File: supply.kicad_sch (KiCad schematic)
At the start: 93 parts, among them IC12 74HC00PW, IC13 SN74LVC1G126DCKR, IC4 TPS7A0518PDBVT, J12 533980471, T3 BSS138APW, U1 LM3671MF-3.3/NOPB, U2 LM62440-Q1, U3 SN74LXC1T45DBVR, U5 LM3671MF-3.3/NOPB, U6 SIC477ED-T1-GE3

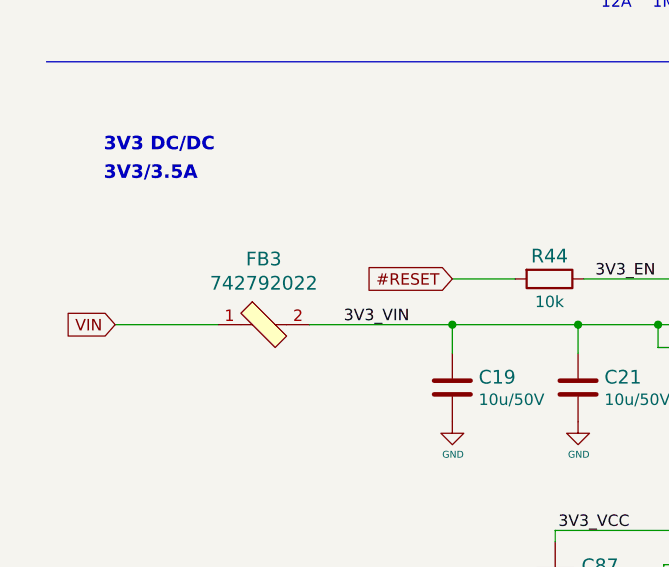
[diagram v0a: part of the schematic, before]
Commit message: Replaced 742792022 ferrites with 74279220181 for higher current capability
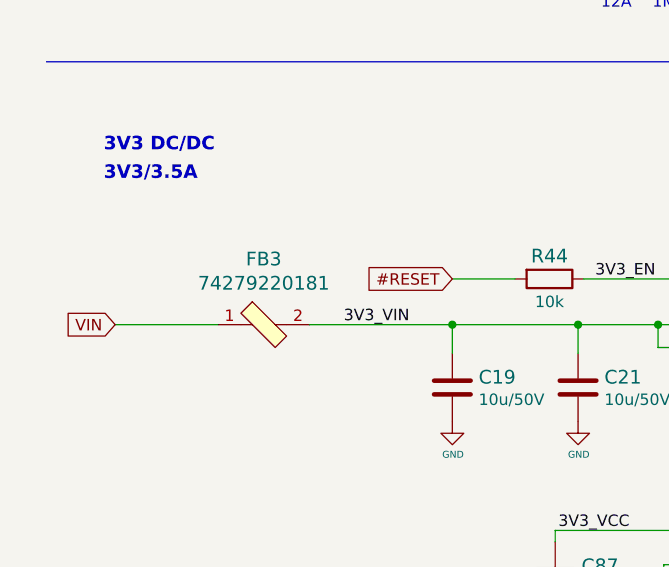
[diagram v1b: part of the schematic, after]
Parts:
- FB3: value 742792022 -> 74279220181; symbol jetson-nano-baseboard:742792022 -> jetson-nano-baseboard:74279220181; MPN 742792022 -> 74279220181
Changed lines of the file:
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@@
     (pin "1")
   )
-  (symbol (lib_id "jetson-nano-baseboard:742792022") (at 40.64 136.525 0) (unit 1)
+  (symbol (lib_id "jetson-nano-baseboard:74279220181") (at 40.64 136.525 0) (unit 1)
     (in_bom yes) (on_board yes)
     (property "Reference" "FB3" (id 0) (at 40.64 129.2352 0)
       (effects (font (size 1.524 1.524)))
     )
-    (property "Value" "742792022" (id 1) (at 40.64 131.9276 0)
+    (property "Value" "74279220181" (id 1) (at 40.64 131.9276 0)
       (effects (font (size 1.524 1.524)))
     )
@@
       (effects (font (size 1.524 1.524)) (justify left) hide)
     )
-    (property "Datasheet" "https://www.we-online.com/katalog/datasheet/742792022.pdf" (id 3) (at 45.72 128.905 0)
+    (property "Datasheet" "https://www.we-online.com/components/products/datasheet/74279220181.pdf" (id 3) (at 45.72 128.905 0)
       (effects (font (size 1.524 1.524)) (justify left) hide)
     )
-    (property "MPN" "742792022" (id 4) (at 45.72 123.825 0)
+    (property "MPN" "74279220181" (id 4) (at 45.72 123.825 0)
       (effects (font (size 1.524 1.524)) (justify left) hide)
     )

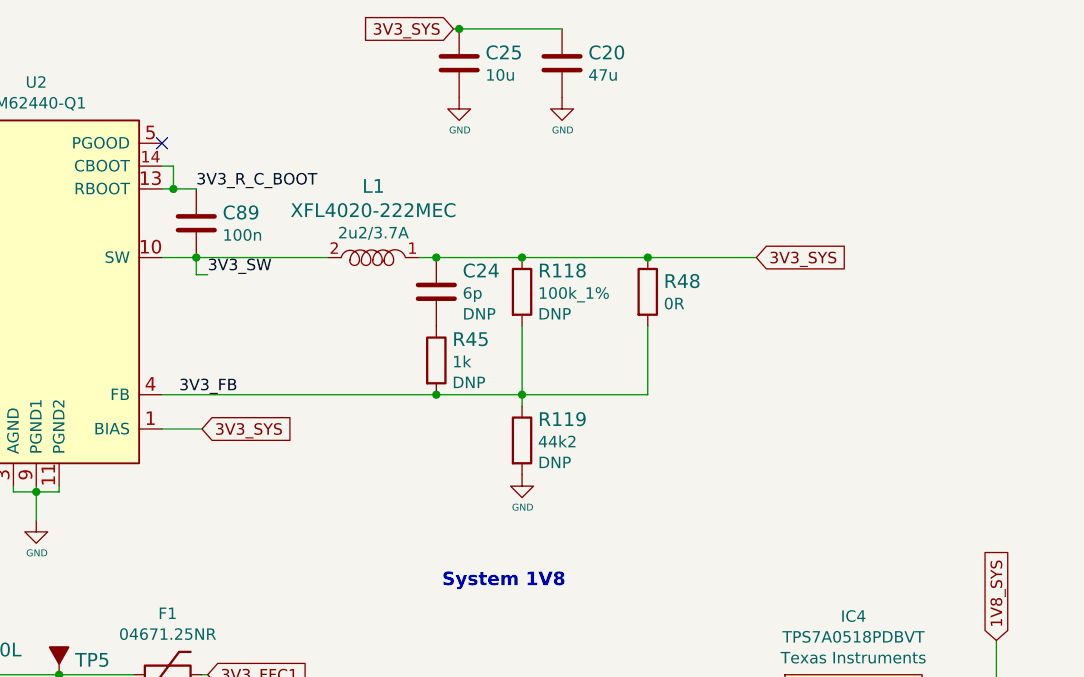
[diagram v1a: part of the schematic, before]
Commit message: Added resistor between RBOOT and CBOOT on 3V3_SYS regulator for reduced EMI
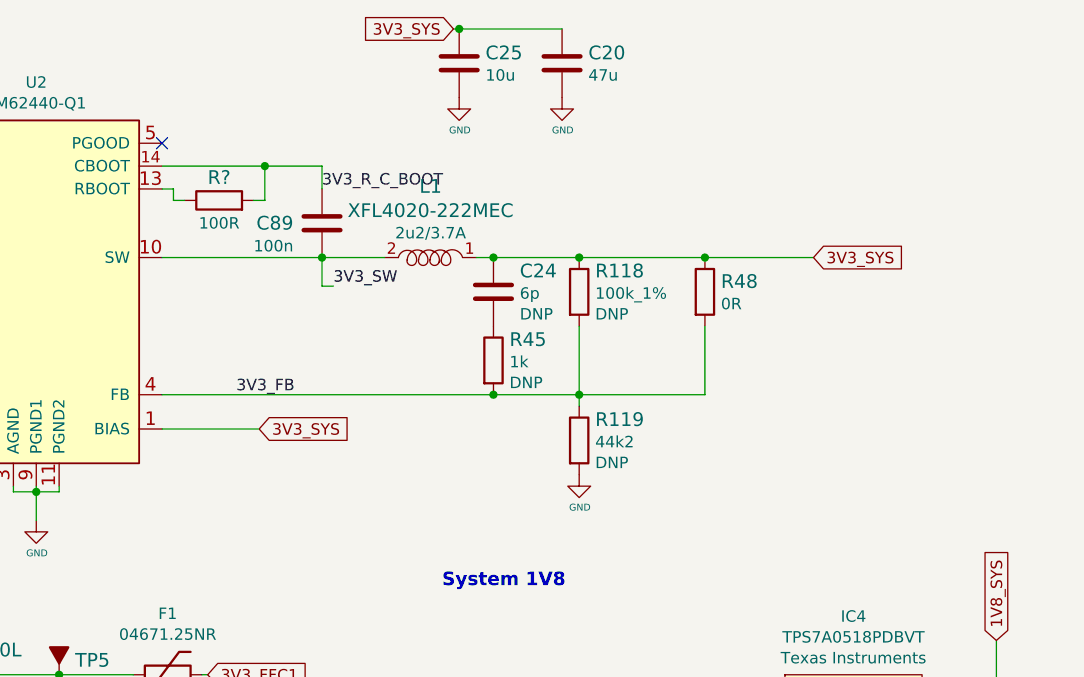
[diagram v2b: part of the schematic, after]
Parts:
- added R?: R_100R_0402, antmicro-footprints:0402-res, symbol antmicroResistors0402:R_100R_0402
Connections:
- net 3V3_R_C_BOOT: now also R?.2; no longer U2.13 (RBOOT)
- new net: R?.1, U2.13 (RBOOT)
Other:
- moved on the sheet: C24, C89, L1, R118, R119, R45, R48

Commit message: Added CAN interface
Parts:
- R?: footprint antmicro-footprints:0402-res -> jetson-nano-baseboard-footprints:0402-res; symbol antmicroResistors0402:R_100R_0402 -> jetson-nano-baseboard:R_100R_0402
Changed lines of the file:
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@@
     (pin "2")
   )
-  (symbol (lib_id "antmicroResistors0402:R_100R_0402") (at 120.015 137.795 0) (unit 1)
+  (symbol (lib_id "jetson-nano-baseboard:R_100R_0402") (at 120.015 137.795 0) (unit 1)
     (in_bom yes) (on_board yes)
     (property "Reference" "R?" (id 0) (at 120.015 135.255 0)
@@
       (effects (font (size 1.524 1.524)) hide)
     )
-    (property "Footprint" "antmicro-footprints:0402-res" (id 2) (at 125.095 132.715 0)
+    (property "Footprint" "jetson-nano-baseboard-footprints:0402-res" (id 2) (at 125.095 132.715 0)
       (effects (font (size 1.524 1.524)) (justify left) hide)
     )

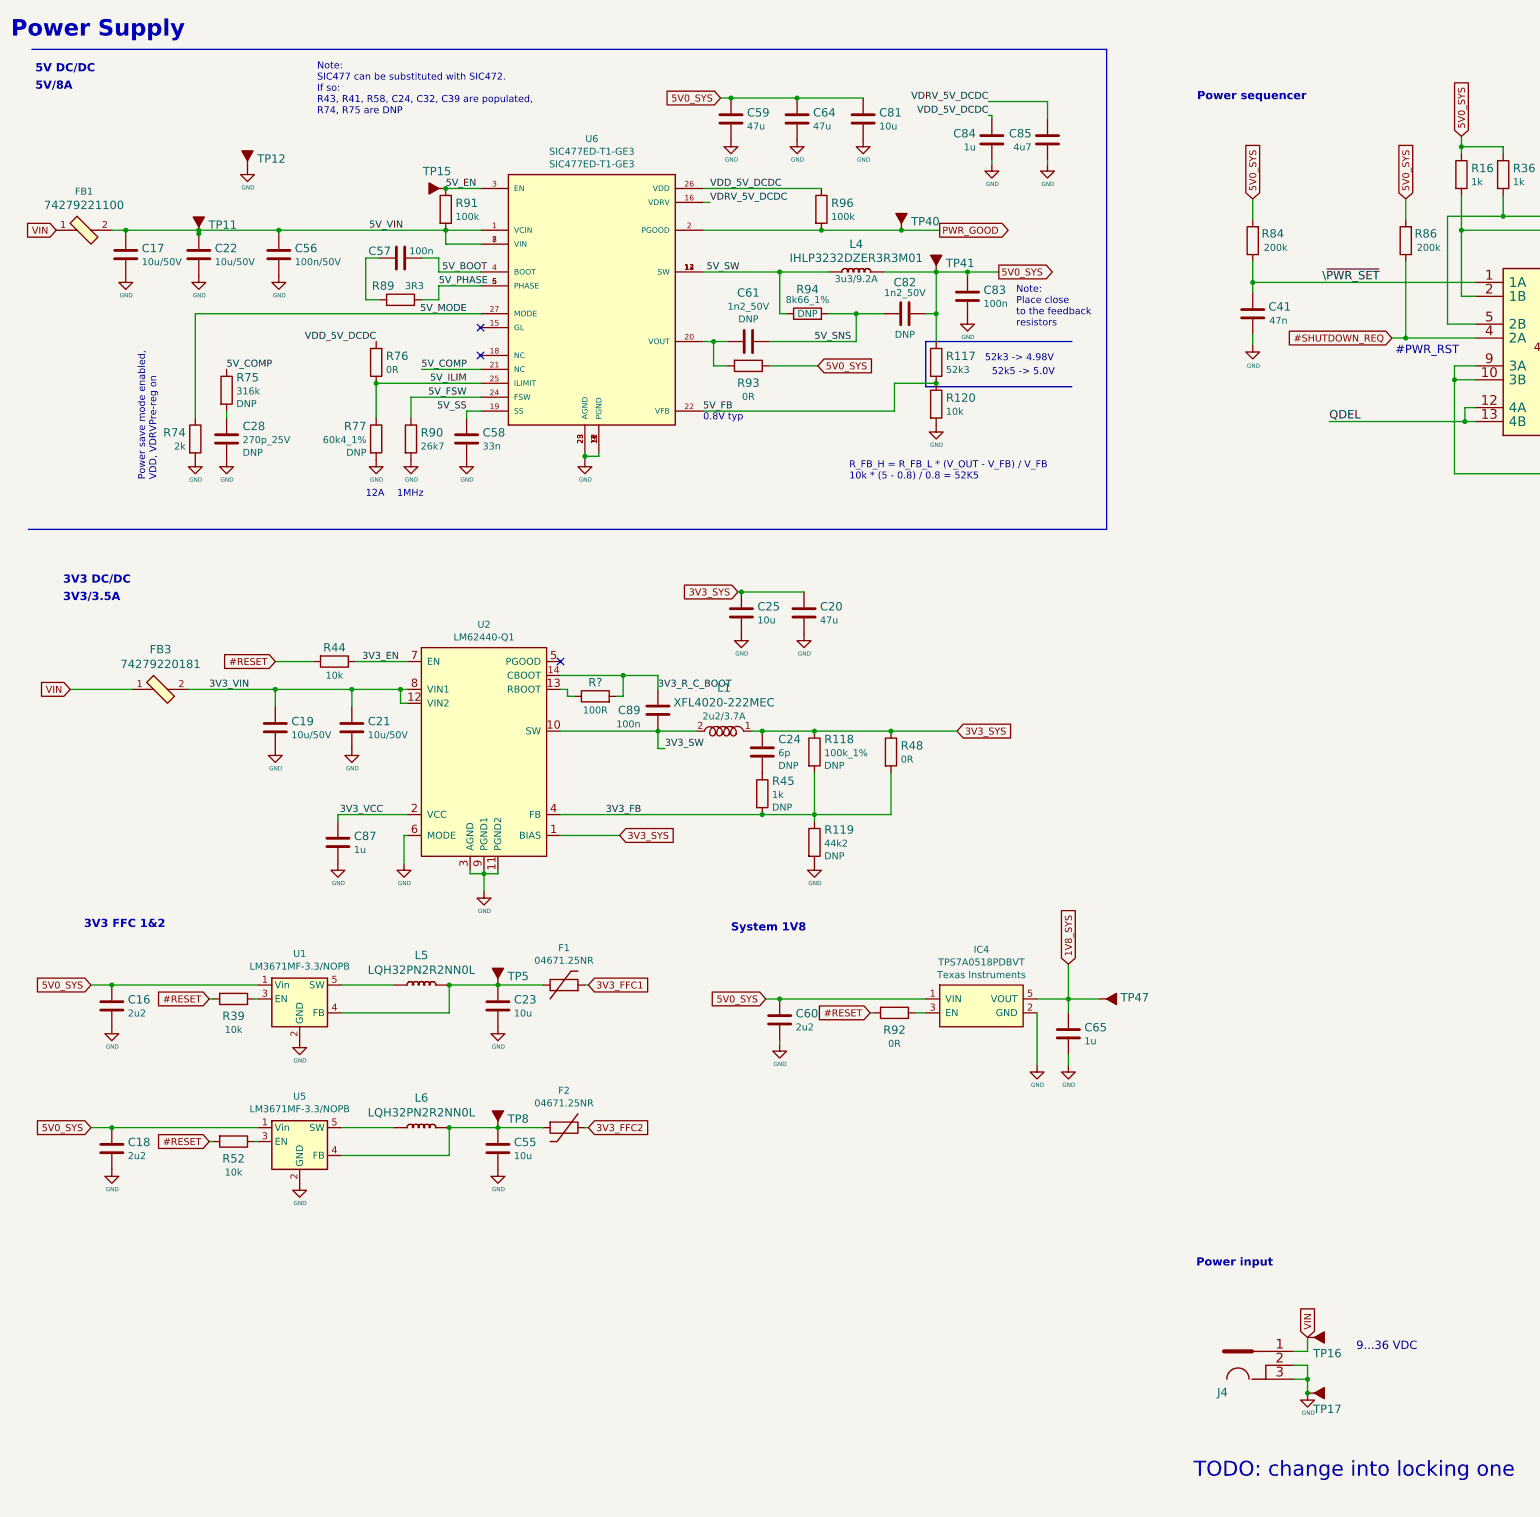
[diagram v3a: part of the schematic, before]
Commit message: Improved input protection - added TVSes, reverse polarity protection and input fuse
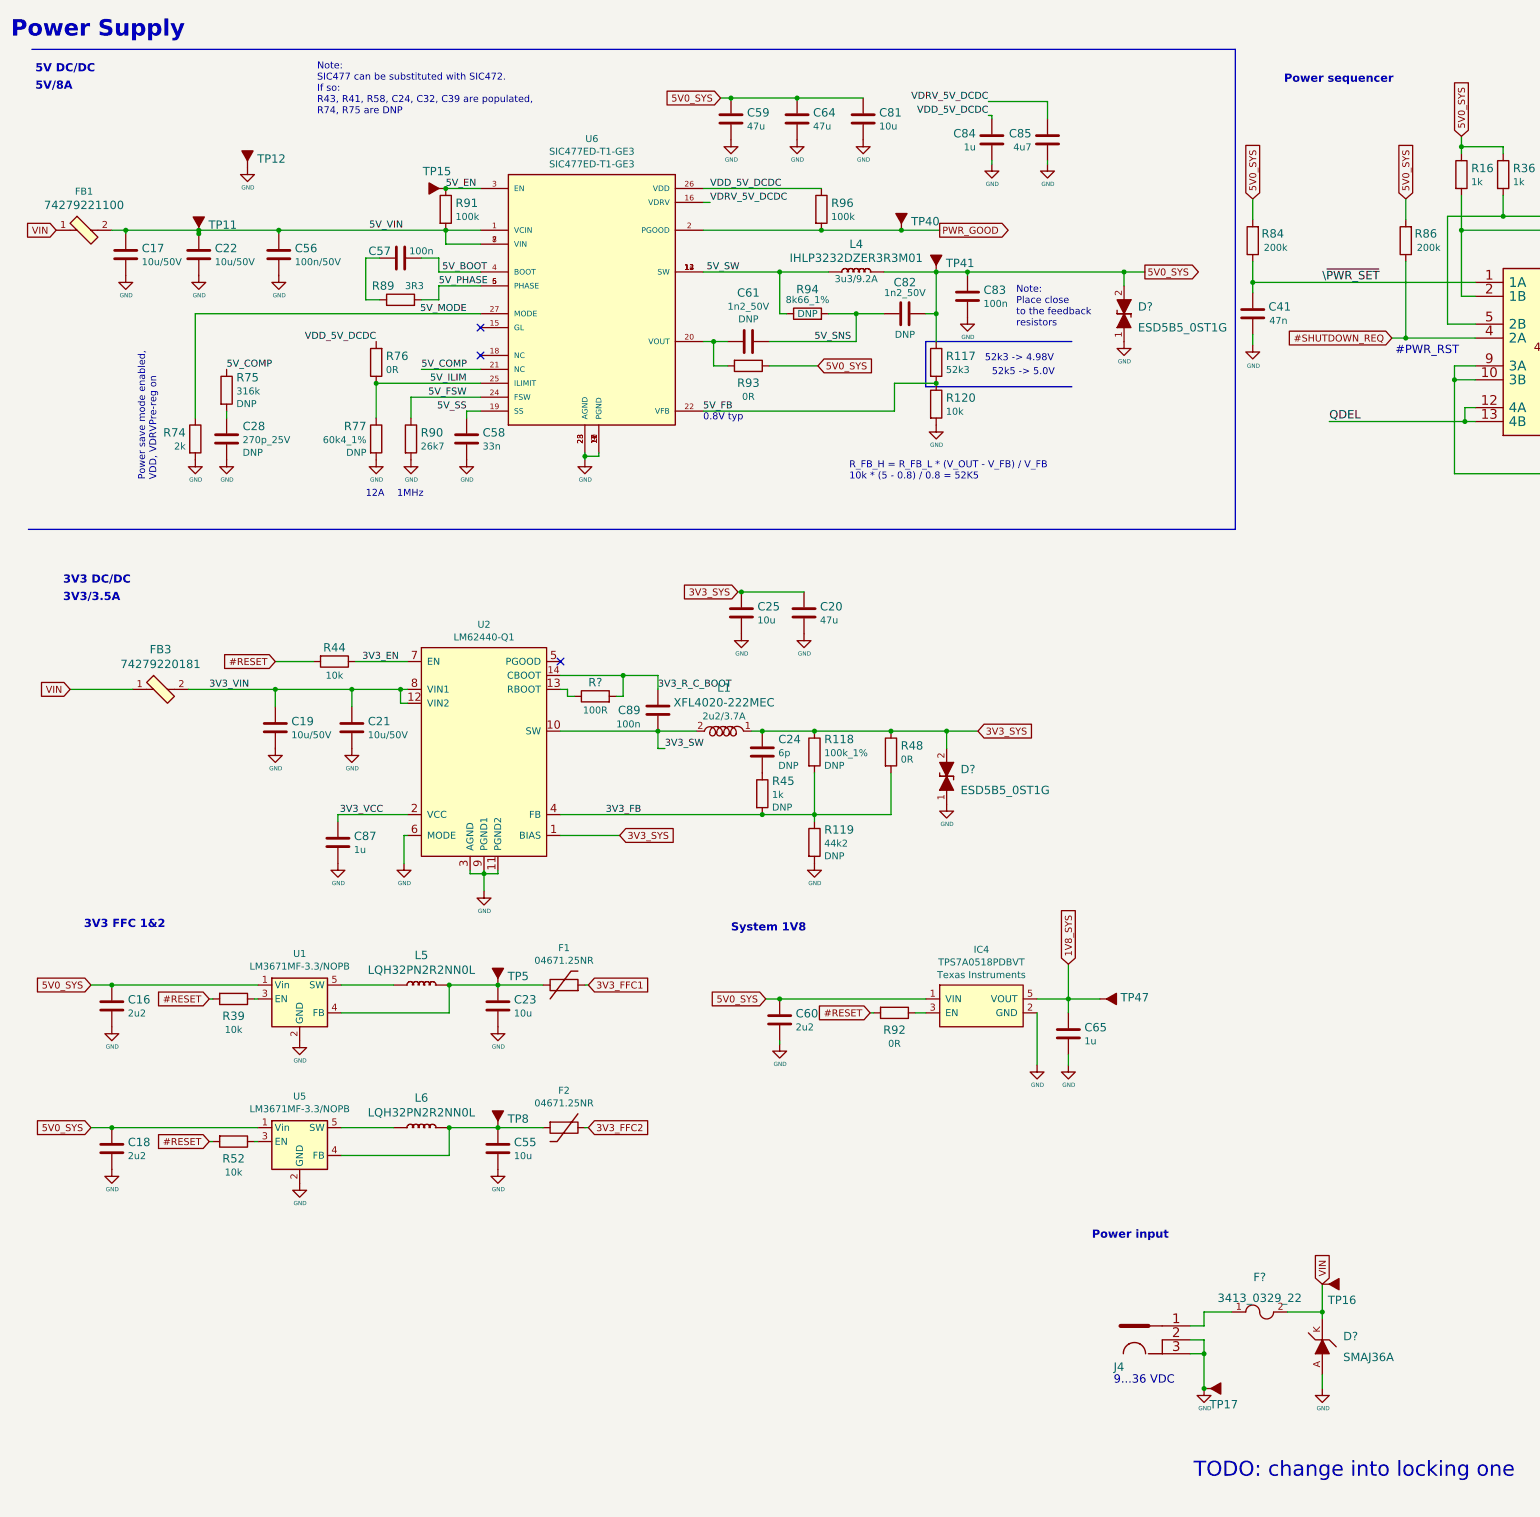
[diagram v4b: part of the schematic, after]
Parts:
- added D?: SMAJ36A, jetson-nano-baseboard-footprints:DO-214AC, symbol jetson-nano-baseboard:SMAJ36A
- added D? (x2): ESD5B5_0ST1G, jetson-nano-baseboard-footprints:SOD-523, symbol jetson-nano-baseboard:ESD5B5_0ST1G
- added F?: 3413_0329_22, jetson-nano-baseboard-footprints:1206, symbol jetson-nano-baseboard:3413_0329_22
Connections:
- net 3V3_SYS: now also D?.2
- net 5V0_SYS: now also D?.2
- net GND: now also D?.1, D?.1, D?.A
- net VIN: now also D?.K, F?.2; no longer J4.1
- new net: F?.1, J4.1
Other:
- moved on the sheet: J4, TP16, TP17

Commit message: Add some todos
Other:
- note added: "TODO: change to SMAJ33"
- note added: "TODO: check with SMB in larger package"
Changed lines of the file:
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@@
+    (effects (font (size 1.27 1.27)) (justify left bottom))
+  )
+  (text "TODO: check with SMB in larger package" (at 257.175 267.97 0)
     (effects (font (size 1.27 1.27)) (justify left bottom))
   )
@@
     (effects (font (size 1.4986 1.4986) (thickness 0.2997) bold) (justify left bottom))
   )
+  (text "TODO: change to SMAJ33" (at 257.175 264.795 0)
+    (effects (font (size 1.27 1.27)) (justify left bottom))
+  )
   (text "System 1V8" (at 144.78 180.975 0)
